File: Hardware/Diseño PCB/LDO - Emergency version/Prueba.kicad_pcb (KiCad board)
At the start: 2 copper layers, 99.4 x 209.5 mm, 132 parts, among them Q1 BC547, Q10 BC547, Q11 BC557, Q12 BC547, Q13 BC557, Q14 BC547, Q15 BC557, Q16 BC547, Q17 BC547, Q18 BC557, Q19 IRF4905, Q2 BC547, Q3 BC557, Q39 BC547, Q4 BC547, Q40 BC547, Q41 BC557, Q42 BC547, Q43 BC557, Q44 BC547, Q45 BC547, Q46 BC547, Q47 BC557, Q48 BC547, Q49 BC557, Q5 BC557, Q50 BC547, Q51 BC557, Q52 BC547, Q53 BC557, Q54 BC547, Q55 BC547, Q56 BC557, Q57 IRF4905, Q6 BC547, Q7 BC547, Q8 BC547, Q9 BC557, U1 LM324, U2 TL431LP, U5 LM324, U6 TL431LP

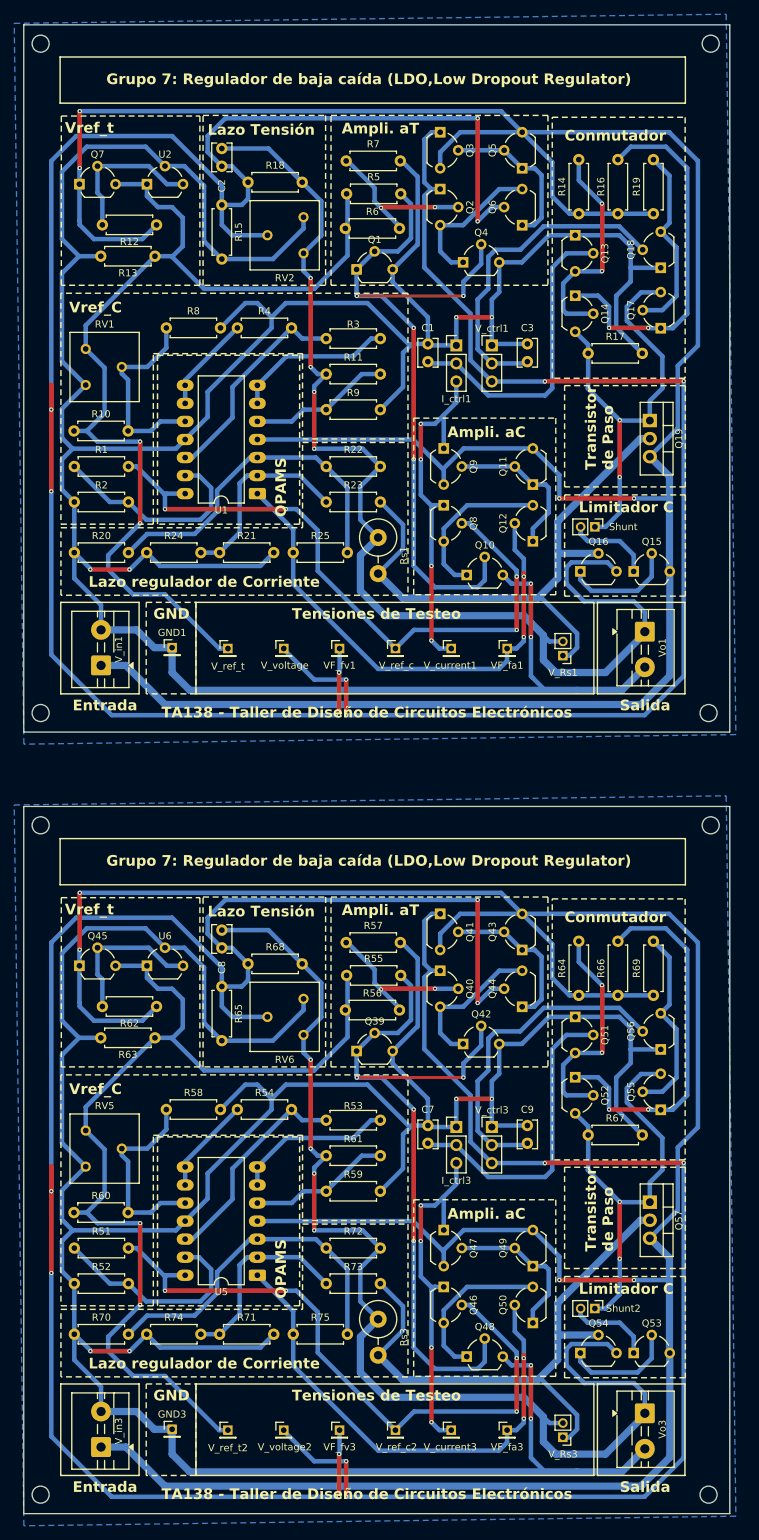
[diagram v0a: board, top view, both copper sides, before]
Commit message: CHK3: Agregue emergency version , pistas y esquematico al informe
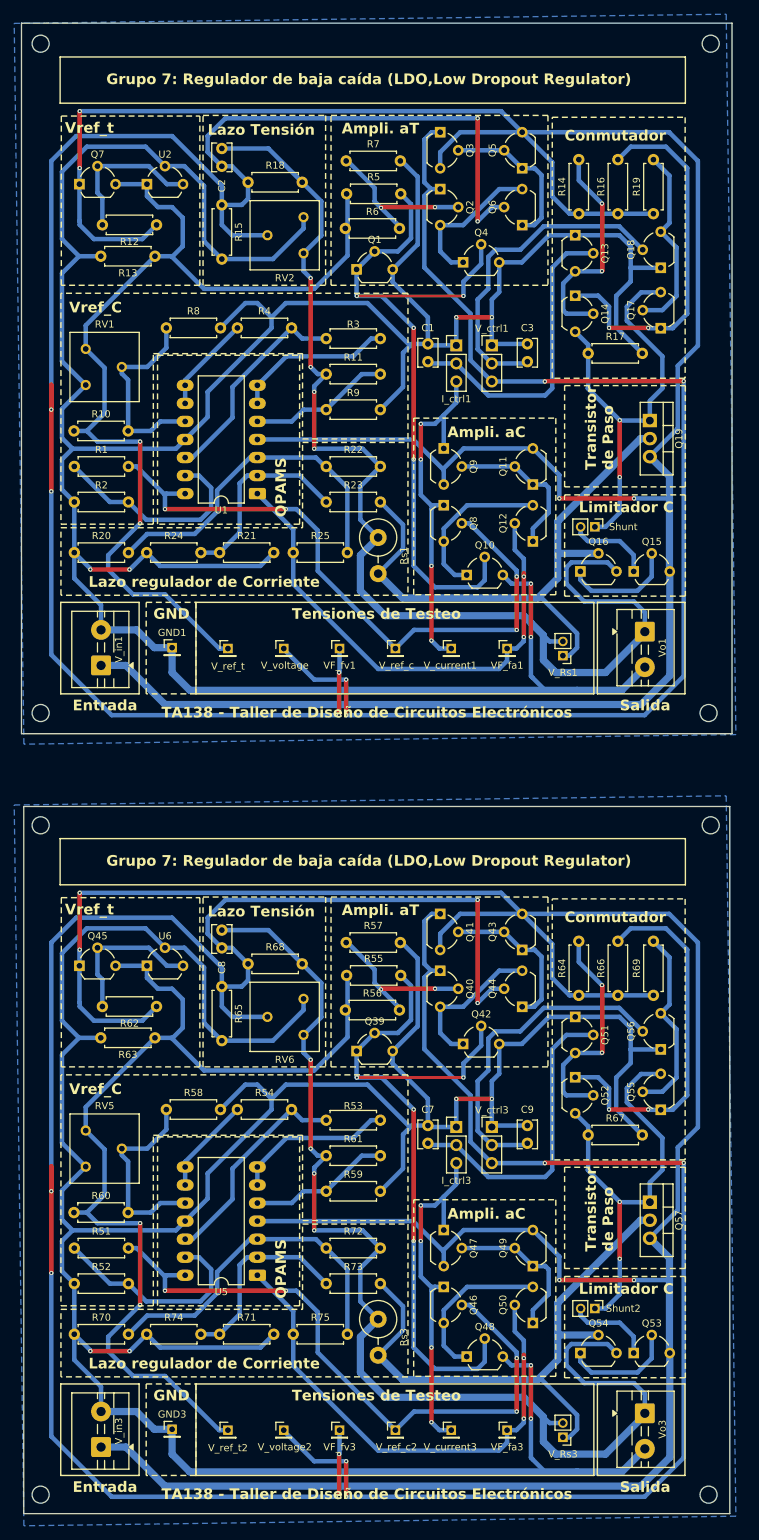
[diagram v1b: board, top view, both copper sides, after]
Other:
- board size 99.4 x 209.5 mm -> 100 x 209.8 mm
